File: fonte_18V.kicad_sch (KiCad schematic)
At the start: 8 parts

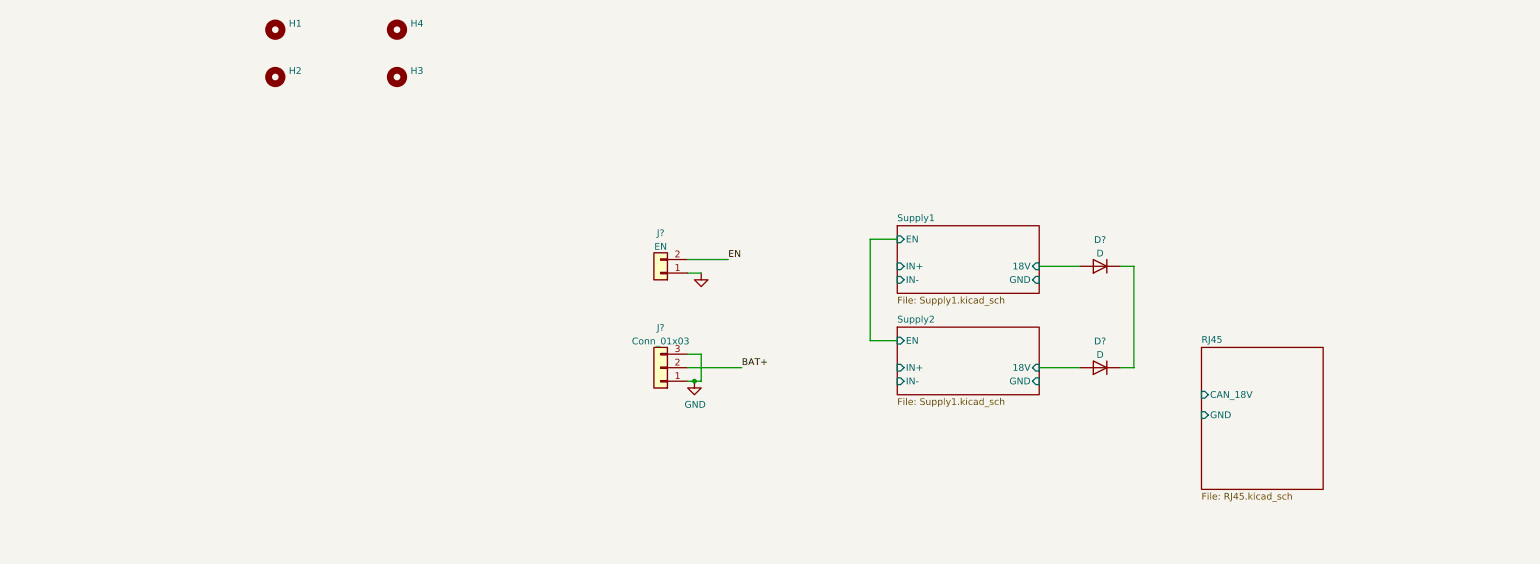
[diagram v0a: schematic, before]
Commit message: Organize schematics for better visualization
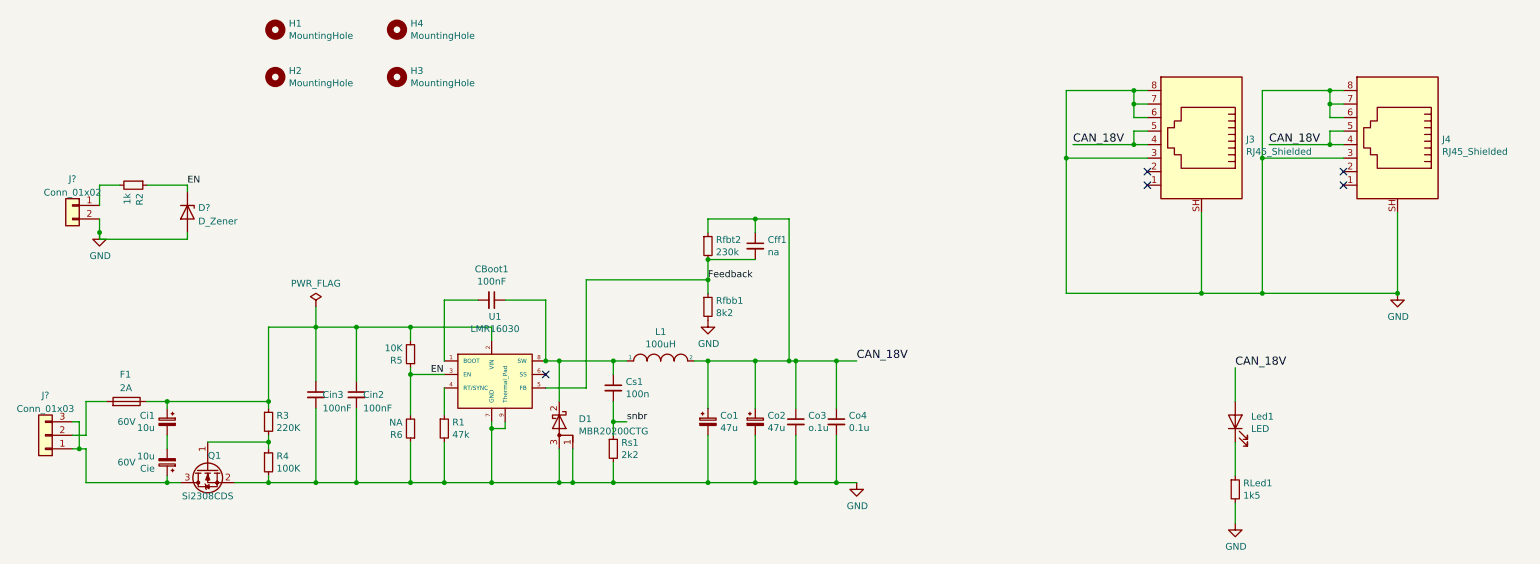
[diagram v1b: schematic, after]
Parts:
- removed D? (x2): D, symbol Device:D
- removed J?: EN, Connector_Phoenix_MSTB:PhoenixContact_MSTBA_2,5_2-G-5,08_1x02_P5.08mm_Horizontal, symbol Connector_Generic:Conn_01x02
- removed J?: Conn_01x03, symbol Connector_Generic:Conn_01x03
- added CBoot1, Cin2, Cin3: 100nF, Capacitor_SMD:C_0805_2012Metric_Pad1.15x1.40mm_HandSolder, symbol fonte_18V-rescue:C_Small-Device
- added Cff1: na, Capacitor_SMD:C_0805_2012Metric_Pad1.15x1.40mm_HandSolder, symbol fonte_18V-rescue:C_Small-Device
- added Ci1, Cie: 10u, Capacitor_THT:CP_Radial_D5.0mm_P2.50mm, symbol Device:C_Polarized_Small
- added Co1, Co2: 47u, Capacitor_THT:CP_Radial_D5.0mm_P2.50mm, symbol Device:C_Polarized_Small
- added Co3: o.1u, Capacitor_SMD:C_0805_2012Metric_Pad1.15x1.40mm_HandSolder, symbol fonte_18V-rescue:C_Small-Device
- added Co4: 0.1u, Capacitor_SMD:C_0805_2012Metric_Pad1.15x1.40mm_HandSolder, symbol fonte_18V-rescue:C_Small-Device
- added Cs1: 100n, Capacitor_SMD:C_0805_2012Metric_Pad1.15x1.40mm_HandSolder, symbol fonte_18V-rescue:C_Small-Device
- added D1: MBR20200CTG, Package_TO_SOT_THT:TO-220-3_Horizontal_TabDown_SMD, symbol fonte_18V-rescue:D_Schottky_AKA-Device
- added D?: D_Zener, symbol Device:D_Zener
- added F1: 2A, KicadZeniteSolarLibrary18:Fuse_Holder_5x20, symbol fonte_18V-rescue:Fuse-Device
- added J3, J4: RJ45_Shielded, MFP19RJ45:RJ45_YH59_01, symbol Connector:RJ45_Shielded
- added J?: Conn_01x03, symbol Connector_Generic:Conn_01x03
- added J?: Conn_01x02, symbol Connector_Generic:Conn_01x02
- added L1: 100uH, Inductor_THT:L_Radial_D21.0mm_P19.00mm, symbol fonte_18V-rescue:INDUCTOR-pspice
- added Led1: LED, LED_SMD:LED_0805_2012Metric_Pad1.15x1.40mm_HandSolder, symbol fonte_18V-rescue:LED-Device
- added Q1: Si2308CDS, Package_TO_SOT_SMD:SOT-23, symbol Device:Q_NMOS_GSD
- added R1: 47k, Resistor_SMD:R_0805_2012Metric_Pad1.15x1.40mm_HandSolder, symbol fonte_18V-rescue:R_Small-Device
- added R2: 1k, Resistor_SMD:R_0805_2012Metric_Pad1.15x1.40mm_HandSolder, symbol fonte_18V-rescue:R_Small-Device
- added R3: 220K, Resistor_SMD:R_0805_2012Metric_Pad1.15x1.40mm_HandSolder, symbol fonte_18V-rescue:R_Small-Device
- added R4: 100K, Resistor_SMD:R_0805_2012Metric_Pad1.15x1.40mm_HandSolder, symbol fonte_18V-rescue:R_Small-Device
- added R5: 10K, Resistor_SMD:R_0805_2012Metric_Pad1.15x1.40mm_HandSolder, symbol fonte_18V-rescue:R_Small-Device
- added R6: NA, Resistor_SMD:R_0805_2012Metric_Pad1.15x1.40mm_HandSolder, symbol fonte_18V-rescue:R_Small-Device
- added RLed1: 1k5, Resistor_SMD:R_0805_2012Metric_Pad1.15x1.40mm_HandSolder, symbol fonte_18V-rescue:R_Small-Device
- added Rfbb1: 8k2, Resistor_SMD:R_0805_2012Metric_Pad1.15x1.40mm_HandSolder, symbol fonte_18V-rescue:R_Small-Device
- added Rfbt2: 230k, Resistor_SMD:R_0805_2012Metric_Pad1.15x1.40mm_HandSolder, symbol fonte_18V-rescue:R_Small-Device
- added Rs1: 2k2, Resistor_SMD:R_0805_2012Metric_Pad1.15x1.40mm_HandSolder, symbol fonte_18V-rescue:R_Small-Device
- added U1: LMR16030, Package_SO:Texas_R-PDSO-G8_EP2.95x4.9mm_Mask2.4x3.1mm_ThermalVias, symbol fonte_18V-rescue:LMR16030-zenite_fonte
- H1, H2, H3, H4: value (none) -> MountingHole; footprint (none) -> MountingHole:MountingHole_3.2mm_M3
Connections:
- net EN: now also D?.1 (K), R2.1, R5.1, R6.2, U1.3 (EN)
- net GND: now also Cin2.2, Cin3.2, Co1.2, Co2.2, Co3.2, Co4.2, D1.1 (A), D1.3 (A), D?.2 (A), J3.3, J3.6, J3.7, J3.8, J3.SH, J4.3, J4.6, J4.7, J4.8, J4.SH, J?.2 (Pin_2), Q1.2 (S), R1.2, R4.2, R6.1, RLed1.2, Rfbb1.2, Rs1.2, U1.7 (GND), U1.9 (Thermal_Pad)
- new net: R1.1, U1.4 (RT/SYNC)
- new net: CBoot1.1, Cs1.1, D1.2 (K), L1.1, U1.8 (SW)
- new net: CBoot1.2, U1.1 (BOOT)
- new net: Ci1.1, Cin2.1, Cin3.1, F1.1, R3.1, R5.2, U1.2 (VIN)
- new net: F1.2, J?.2 (Pin_2)
- new net: Led1.1 (K), RLed1.1
- new net: Q1.1 (G), R3.2, R4.1
- new net: Cie.1, J?.1 (Pin_1), J?.3 (Pin_3), Q1.3 (D)
- new net: J?.1 (Pin_1), R2.2
- new net: Ci1.2, Cie.2
- new net CAN_18V: Cff1.1, Co1.1, Co2.1, Co3.1, Co4.1, J3.4, J3.5, J4.4, J4.5, L1.2, Led1.2 (A), Rfbt2.1
- new net Feedback: Cff1.2, Rfbb1.1, Rfbt2.2, U1.5 (FB)
- new net snbr: Cs1.2, Rs1.1
- no-connect marks 0 -> 5
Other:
- removed sheet RJ45
- removed sheet Supply1
- removed sheet Supply2

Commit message: temp
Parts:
- removed D1: MBR20200CTG, Package_TO_SOT_THT:TO-220-3_Horizontal_TabDown_SMD, symbol fonte_18V-rescue:D_Schottky_AKA-Device
- removed F1: 2A, KicadZeniteSolarLibrary18:Fuse_Holder_5x20, symbol fonte_18V-rescue:Fuse-Device
- added D102: MBR340, Diode_SMD:D_SMA_Handsoldering, symbol Device:D_Schottky
- added D103, D104: B1100, Diode_SMD:D_SMA_Handsoldering, symbol Device:D_Schottky
- added F101: Fuse, KicadZeniteSolarLibrary18:Fuse_Holder_5x20, symbol Device:Fuse
- D101: renamed from D?; value D_Zener -> 4v7; footprint (none) -> Diode_SMD:D_MiniMELF
- J101: renamed from J?; value Conn_01x03 -> IN; footprint (none) -> TerminalBlock:TerminalBlock_bornier-3_P5.08mm
- J102: renamed from J?; footprint (none) -> TerminalBlock:TerminalBlock_bornier-2_P5.08mm
- renumbered Cie to Cie101
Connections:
- net CAN_18V: now also D102.1 (K); no longer Cff1.1, Co1.1, Co2.1, Co3.1, Co4.1, L1.2, Led1.2 (A), Rfbt2.1
- net GND: now also D103.2 (A), D104.2 (A)
- net at CBoot1.1, Cs1.1, L1.1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: now also D103.1 (K), D104.1 (K)
- net at Ci1.1, Cin2.1, Cin3.1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: now also F101.2
- net at J101.2 (Pin_2): now also F101.1
- net at J4.1: now also J3.1
- net at J4.2: now also J3.2
- new net CAN_18V_DIODE: Cff1.1, Co1.1, Co2.1, Co3.1, Co4.1, D102.2 (A), L1.2, Led1.2 (A), Rfbt2.1
- no-connect marks 5 -> 1

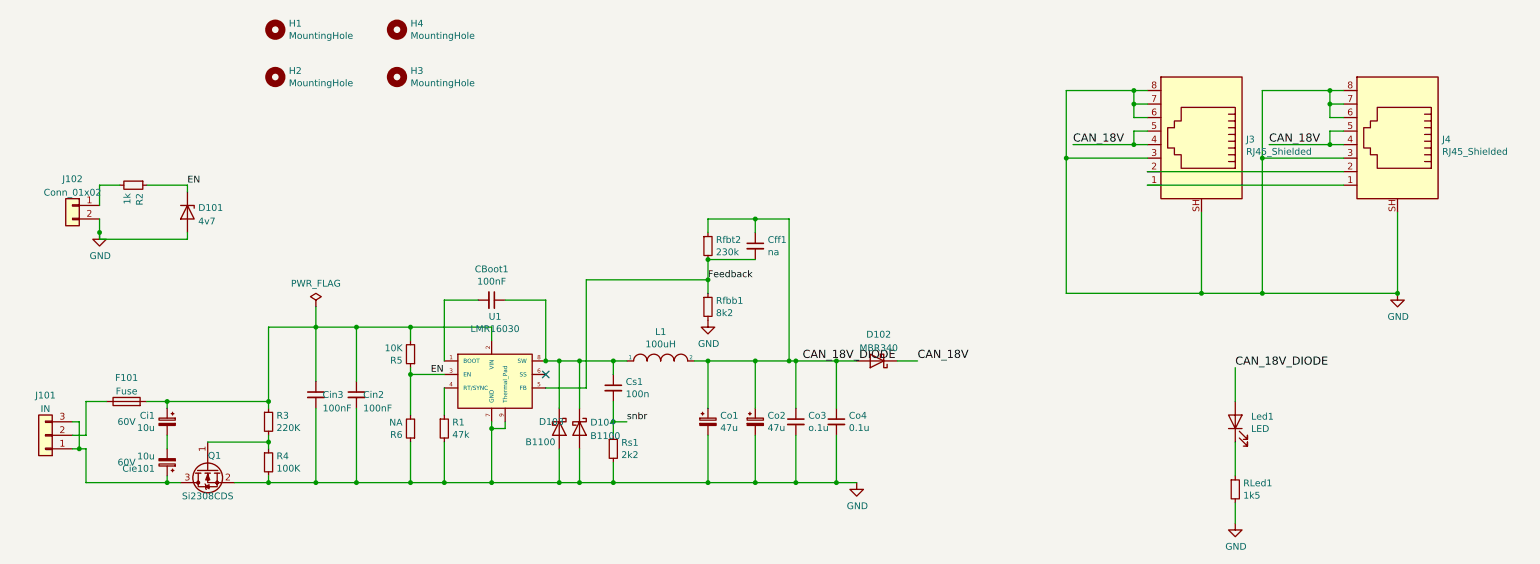
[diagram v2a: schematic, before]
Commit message: Duplicate fonts for redundancy and initialized layout
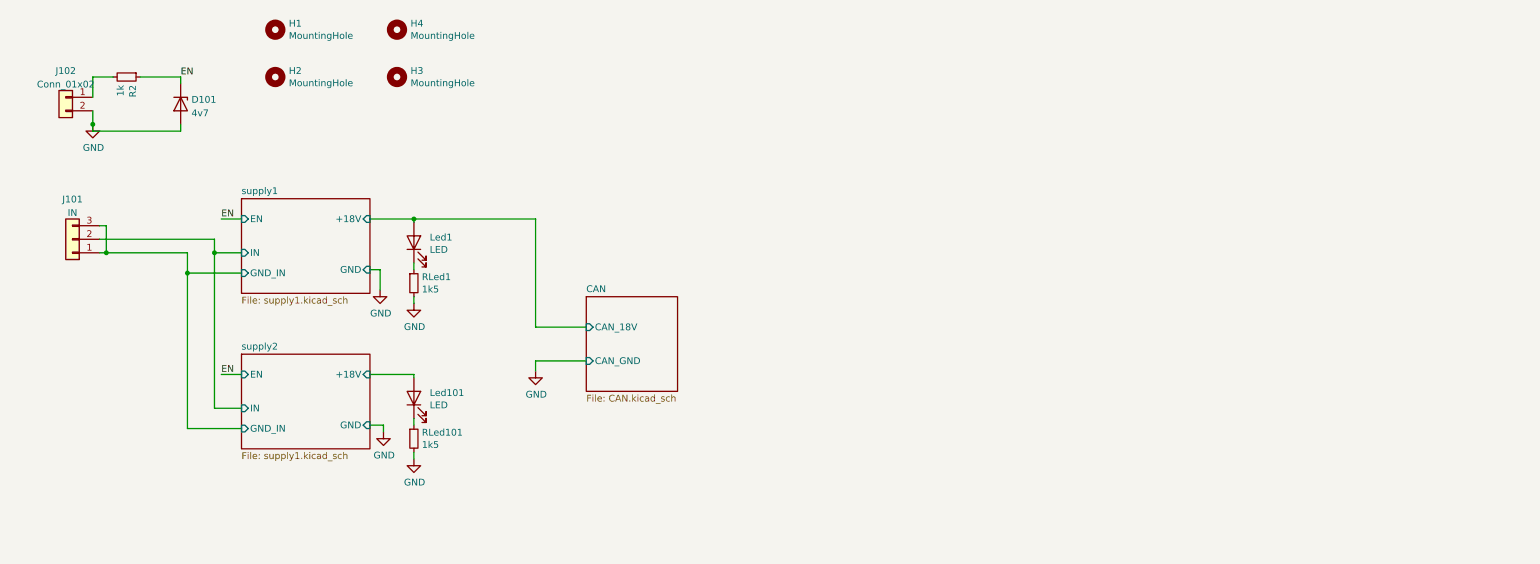
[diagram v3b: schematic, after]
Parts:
- removed CBoot1, Cin2, Cin3: 100nF, Capacitor_SMD:C_0805_2012Metric_Pad1.15x1.40mm_HandSolder, symbol fonte_18V-rescue:C_Small-Device
- removed Cff1: na, Capacitor_SMD:C_0805_2012Metric_Pad1.15x1.40mm_HandSolder, symbol fonte_18V-rescue:C_Small-Device
- removed Ci1, Cie101: 10u, Capacitor_THT:CP_Radial_D5.0mm_P2.50mm, symbol Device:C_Polarized_Small
- removed Co1, Co2: 47u, Capacitor_THT:CP_Radial_D5.0mm_P2.50mm, symbol Device:C_Polarized_Small
- removed Co3: o.1u, Capacitor_SMD:C_0805_2012Metric_Pad1.15x1.40mm_HandSolder, symbol fonte_18V-rescue:C_Small-Device
- removed Co4: 0.1u, Capacitor_SMD:C_0805_2012Metric_Pad1.15x1.40mm_HandSolder, symbol fonte_18V-rescue:C_Small-Device
- removed Cs1: 100n, Capacitor_SMD:C_0805_2012Metric_Pad1.15x1.40mm_HandSolder, symbol fonte_18V-rescue:C_Small-Device
- removed D102: MBR340, Diode_SMD:D_SMA_Handsoldering, symbol Device:D_Schottky
- removed D103, D104: B1100, Diode_SMD:D_SMA_Handsoldering, symbol Device:D_Schottky
- removed F101: Fuse, KicadZeniteSolarLibrary18:Fuse_Holder_5x20, symbol Device:Fuse
- removed J3, J4: RJ45_Shielded, MFP19RJ45:RJ45_YH59_01, symbol Connector:RJ45_Shielded
- removed L1: 100uH, Inductor_THT:L_Radial_D21.0mm_P19.00mm, symbol fonte_18V-rescue:INDUCTOR-pspice
- removed Q1: Si2308CDS, Package_TO_SOT_SMD:SOT-23, symbol Device:Q_NMOS_GSD
- removed R1: 47k, Resistor_SMD:R_0805_2012Metric_Pad1.15x1.40mm_HandSolder, symbol fonte_18V-rescue:R_Small-Device
- removed R3: 220K, Resistor_SMD:R_0805_2012Metric_Pad1.15x1.40mm_HandSolder, symbol fonte_18V-rescue:R_Small-Device
- removed R4: 100K, Resistor_SMD:R_0805_2012Metric_Pad1.15x1.40mm_HandSolder, symbol fonte_18V-rescue:R_Small-Device
- removed R5: 10K, Resistor_SMD:R_0805_2012Metric_Pad1.15x1.40mm_HandSolder, symbol fonte_18V-rescue:R_Small-Device
- removed R6: NA, Resistor_SMD:R_0805_2012Metric_Pad1.15x1.40mm_HandSolder, symbol fonte_18V-rescue:R_Small-Device
- removed Rfbb1: 8k2, Resistor_SMD:R_0805_2012Metric_Pad1.15x1.40mm_HandSolder, symbol fonte_18V-rescue:R_Small-Device
- removed Rfbt2: 230k, Resistor_SMD:R_0805_2012Metric_Pad1.15x1.40mm_HandSolder, symbol fonte_18V-rescue:R_Small-Device
- removed Rs1: 2k2, Resistor_SMD:R_0805_2012Metric_Pad1.15x1.40mm_HandSolder, symbol fonte_18V-rescue:R_Small-Device
- removed U1: LMR16030, Package_SO:Texas_R-PDSO-G8_EP2.95x4.9mm_Mask2.4x3.1mm_ThermalVias, symbol fonte_18V-rescue:LMR16030-zenite_fonte
- added Led101: LED, LED_SMD:LED_0805_2012Metric_Pad1.15x1.40mm_HandSolder, symbol fonte_18V-rescue:LED-Device
- added RLed101: 1k5, Resistor_SMD:R_0805_2012Metric_Pad1.20x1.40mm_HandSolder, symbol fonte_18V-rescue:R_Small-Device
- R2, RLed1: footprint Resistor_SMD:R_0805_2012Metric_Pad1.15x1.40mm_HandSolder -> Resistor_SMD:R_0805_2012Metric_Pad1.20x1.40mm_HandSolder
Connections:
- net GND: now also RLed101.2
- net supply1/GND_IN: now reaches J101.1 (Pin_1), J101.3 (Pin_3)
- net supply1/IN: now reaches J101.2 (Pin_2)
- net CAN_18V_DIODE renamed CAN/CAN_18V
- new net: Led101.1 (K), RLed101.1
- new net supply2/+18V: Led101.2 (A)
- no-connect marks 1 -> 0
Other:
- added sheet CAN (CAN.kicad_sch)
- added sheet supply1 (supply1.kicad_sch)
- added sheet supply2 (supply1.kicad_sch)
- moved on the sheet: D101, J102, Led1, R2, RLed1

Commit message: almost finished
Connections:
- net CAN/CAN_18V: no longer Led1.2 (A)
- net supply2/+18V renamed supply2/LED
- new net supply1/LED: Led1.2 (A)
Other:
- sheet supply1 ports: added LED; removed none
- sheet supply2 ports: added LED; removed none
- moved on the sheet: Led1, Led101, RLed1, RLed101
